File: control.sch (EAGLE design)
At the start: 63 parts

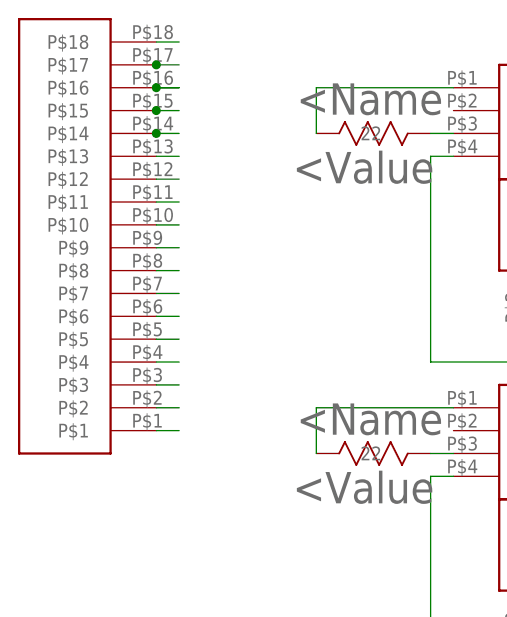
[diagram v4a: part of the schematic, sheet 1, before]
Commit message: Revert "adds flex connector"
This reverts commit c0465f8f5036756819879aef16fe9e16a98b933a.
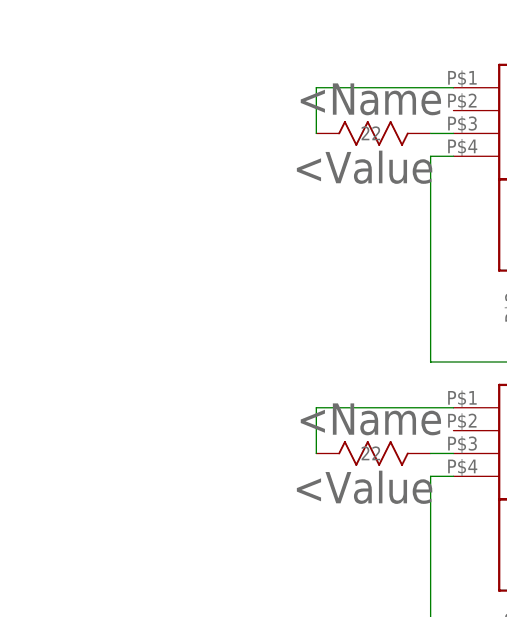
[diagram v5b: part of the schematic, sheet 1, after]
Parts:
- U$39: value SFV18R-3STBE1HLF -> MOTORCONNECTOR; device Smile_Shade:SFV18R-3STBE1HLF -> Smile_Shade:MOTORCONNECTOR
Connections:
- net LEDSTR_1: no longer U$39.P$18
- net LEDSTR_10: no longer U$39.P$9
- net LEDSTR_11: no longer U$39.P$10
- net LEDSTR_12: no longer U$39.P$7
- net LEDSTR_13: no longer U$39.P$6
- net LEDSTR_14: no longer U$39.P$5
- net LEDSTR_15: no longer U$39.P$4
- net LEDSTR_16: no longer U$39.P$3
- net LEDSTR_17: no longer U$39.P$1
- net LEDSTR_18: no longer U$39.P$2
- net LEDSTR_2: no longer U$39.P$17
- net LEDSTR_3: no longer U$39.P$16
- net LEDSTR_4: no longer U$39.P$15
- net LEDSTR_5: no longer U$39.P$12
- net LEDSTR_6: no longer U$39.P$13
- net LEDSTR_7: no longer U$39.P$14
- net LEDSTR_8: no longer U$39.P$11
- net LEDSTR_9: no longer U$39.P$8
- net M1A: now also U$38.MB
- net M1B: now also U$38.MA
- net M2A: now also U$39.MA; no longer U$38.MA
- net M2B: now also U$39.MB; no longer U$38.MB
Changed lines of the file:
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@@
 <part name="U$37" library="Smile_Shade" deviceset="PCA9685PW/Q900" device=""/>
 <part name="U$38" library="Smile_Shade" deviceset="MOTORCONNECTOR" device=""/>
+<part name="U$39" library="Smile_Shade" deviceset="MOTORCONNECTOR" device=""/>
 <part name="U$40" library="LED Driver" deviceset="NUD4011DR2G" device=""/>
 <part name="U$41" library="LED Driver" deviceset="2N7002P" device=""/>
@@
 <part name="U$43" library="LED Driver" deviceset="2N7002P" device=""/>
 <part name="R18" library="LED Driver" deviceset="RC0603FR-0710RL" device=""/>
-<part name="U$39" library="Smile_Shade" deviceset="SFV18R-3STBE1HLF" device=""/>
 </parts>
 <sheets>
@@
 <instance part="U$43" gate="G$1" x="55.88" y="-58.42"/>
 <instance part="R18" gate="A" x="30.48" y="-45.72"/>
-<instance part="U$39" gate="G$1" x="-43.18" y="60.96" rot="R90"/>
 </instances>
 <busses>
@@
 <wire x1="22.86" y1="101.6" x2="25.4" y2="101.6" width="0.1524" layer="91"/>
 </segment>
-<segment>
-<pinref part="U$39" gate="G$1" pin="P$18"/>
-<wire x1="-38.1" y1="106.68" x2="-35.56" y2="106.68" width="0.1524" layer="91"/>
-</segment>
 </net>
 <net name="N$15" class="0">
@@
 <wire x1="73.66" y1="101.6" x2="76.2" y2="101.6" width="0.1524" layer="91"/>
 </segment>
-<segment>
-<wire x1="-38.1" y1="104.14" x2="-35.56" y2="104.14" width="0.1524" layer="91"/>
-<pinref part="U$39" gate="G$1" pin="P$17"/>
-<junction x="-38.1" y="104.14"/>
-</segment>
 </net>
 <net name="N$1" class="0">
@@
 <wire x1="121.92" y1="101.6" x2="124.46" y2="101.6" width="0.1524" layer="91"/>
 </segment>
-<segment>
-<wire x1="-38.1" y1="101.6" x2="-35.56" y2="101.6" width="0.1524" layer="91"/>
-<wire x1="-38.1" y1="101.6" x2="-35.56" y2="101.6" width="0.1524" layer="91"/>
-<pinref part="U$39" gate="G$1" pin="P$16"/>
-<junction x="-38.1" y="101.6"/>
-</segment>
 </net>
 <net name="N$3" class="0">
@@
 <wire x1="172.72" y1="101.6" x2="175.26" y2="101.6" width="0.1524" layer="91"/>
 </segment>
-<segment>
-<wire x1="-38.1" y1="99.06" x2="-35.56" y2="99.06" width="0.1524" layer="91"/>
-<pinref part="U$39" gate="G$1" pin="P$15"/>
-<junction x="-38.1" y="99.06"/>
-</segment>
 </net>
 <net name="N$5" class="0">
@@
 <wire x1="22.86" y1="66.04" x2="25.4" y2="66.04" width="0.1524" layer="91"/>
 </segment>
-<segment>
-<pinref part="U$39" gate="G$1" pin="P$12"/>
-<wire x1="-38.1" y1="91.44" x2="-35.56" y2="91.44" width="0.1524" layer="91"/>
-</segment>
 </net>
 <net name="N$7" class="0">
@@
 <wire x1="73.66" y1="66.04" x2="76.2" y2="66.04" width="0.1524" layer="91"/>
 </segment>
-<segment>
-<pinref part="U$39" gate="G$1" pin="P$13"/>
-<wire x1="-38.1" y1="93.98" x2="-35.56" y2="93.98" width="0.1524" layer="91"/>
-</segment>
 </net>
 <net name="N$9" class="0">
@@
 <wire x1="121.92" y1="66.04" x2="124.46" y2="66.04" width="0.1524" layer="91"/>
 </segment>
-<segment>
-<wire x1="-38.1" y1="96.52" x2="-35.56" y2="96.52" width="0.1524" layer="91"/>
-<pinref part="U$39" gate="G$1" pin="P$14"/>
-<junction x="-38.1" y="96.52"/>
-</segment>
 </net>
 <net name="N$11" class="0">
@@
 <wire x1="172.72" y1="66.04" x2="175.26" y2="66.04" width="0.1524" layer="91"/>
 </segment>
-<segment>
-<pinref part="U$39" gate="G$1" pin="P$11"/>
-<wire x1="-38.1" y1="88.9" x2="-35.56" y2="88.9" width="0.1524" layer="91"/>
-</segment>
 </net>
 <net name="N$13" class="0">
@@
 <wire x1="22.86" y1="30.48" x2="25.4" y2="30.48" width="0.1524" layer="91"/>
 </segment>
-<segment>
-<pinref part="U$39" gate="G$1" pin="P$8"/>
-<wire x1="-38.1" y1="81.28" x2="-35.56" y2="81.28" width="0.1524" layer="91"/>
-</segment>
 </net>
 <net name="N$17" class="0">
@@
 <wire x1="73.66" y1="30.48" x2="76.2" y2="30.48" width="0.1524" layer="91"/>
 </segment>
-<segment>
-<pinref part="U$39" gate="G$1" pin="P$9"/>
-<wire x1="-38.1" y1="83.82" x2="-35.56" y2="83.82" width="0.1524" layer="91"/>
-</segment>
 </net>
 <net name="N$19" class="0">
@@
 <wire x1="121.92" y1="30.48" x2="124.46" y2="30.48" width="0.1524" layer="91"/>
 </segment>
-<segment>
-<pinref part="U$39" gate="G$1" pin="P$10"/>
-<wire x1="-38.1" y1="86.36" x2="-35.56" y2="86.36" width="0.1524" layer="91"/>
-</segment>
 </net>
 <net name="N$21" class="0">
@@
 <wire x1="172.72" y1="30.48" x2="175.26" y2="30.48" width="0.1524" layer="91"/>
 </segment>
-<segment>
-<pinref part="U$39" gate="G$1" pin="P$7"/>
-<wire x1="-38.1" y1="78.74" x2="-35.56" y2="78.74" width="0.1524" layer="91"/>
-</segment>
 </net>
 <net name="N$23" class="0">
@@
 <wire x1="22.86" y1="-5.08" x2="25.4" y2="-5.08" width="0.1524" layer="91"/>
 </segment>
-<segment>
-<pinref part="U$39" gate="G$1" pin="P$6"/>
-<wire x1="-38.1" y1="76.2" x2="-35.56" y2="76.2" width="0.1524" layer="91"/>
-</segment>
 </net>
 <net name="N$25" class="0">
@@
 <wire x1="73.66" y1="-5.08" x2="76.2" y2="-5.08" width="0.1524" layer="91"/>
 </segment>
-<segment>
-<pinref part="U$39" gate="G$1" pin="P$5"/>
-<wire x1="-38.1" y1="73.66" x2="-35.56" y2="73.66" width="0.1524" layer="91"/>
-</segment>
 </net>
 <net name="N$27" class="0">
@@
 <wire x1="121.92" y1="-5.08" x2="124.46" y2="-5.08" width="0.1524" layer="91"/>
 </segment>
-<segment>
-<pinref part="U$39" gate="G$1" pin="P$4"/>
-<wire x1="-38.1" y1="71.12" x2="-35.56" y2="71.12" width="0.1524" layer="91"/>
-</segment>
 </net>
 <net name="N$29" class="0">
@@
 <wire x1="172.72" y1="-5.08" x2="175.26" y2="-5.08" width="0.1524" layer="91"/>
 </segment>
-<segment>
-<pinref part="U$39" gate="G$1" pin="P$3"/>
-<wire x1="-38.1" y1="68.58" x2="-35.56" y2="68.58" width="0.1524" layer="91"/>
-</segment>
 </net>
 <net name="N$31" class="0">
@@
 <wire x1="22.86" y1="-40.64" x2="25.4" y2="-40.64" width="0.1524" layer="91"/>
 </segment>
-<segment>
-<pinref part="U$39" gate="G$1" pin="P$1"/>
-<wire x1="-38.1" y1="63.5" x2="-35.56" y2="63.5" width="0.1524" layer="91"/>
-</segment>
 </net>
 <net name="N$35" class="0">
@@
 <wire x1="73.66" y1="-40.64" x2="76.2" y2="-40.64" width="0.1524" layer="91"/>
 </segment>
-<segment>
-<pinref part="U$39" gate="G$1" pin="P$2"/>
-<wire x1="-38.1" y1="66.04" x2="-35.56" y2="66.04" width="0.1524" layer="91"/>
-</segment>
 </net>
 <net name="N$37" class="0">
@@
 <instance part="C2" gate="A" x="104.14" y="68.58"/>
 <instance part="U$37" gate="G$1" x="213.36" y="43.18"/>
-<instance part="U$38" gate="G$1" x="218.44" y="27.94"/>
+<instance part="U$38" gate="G$1" x="76.2" y="25.4" rot="R180"/>
+<instance part="U$39" gate="G$1" x="218.44" y="27.94"/>
 </instances>
 <busses>
@@
 <segment>
 <wire x1="83.82" y1="30.48" x2="83.82" y2="27.94" width="0.1524" layer="91"/>
+<pinref part="U$38" gate="G$1" pin="MB"/>
+<wire x1="83.82" y1="27.94" x2="81.28" y2="27.94" width="0.1524" layer="91"/>
 <pinref part="U$2" gate="A" pin="1Y"/>
 <wire x1="83.82" y1="30.48" x2="88.9" y2="30.48" width="0.1524" layer="91"/>
@@
 <net name="M2B" class="0">
 <segment>
+<pinref part="U$39" gate="G$1" pin="MB"/>
 <wire x1="213.36" y1="25.4" x2="213.36" y2="22.86" width="0.1524" layer="91"/>
 <pinref part="U$2" gate="A" pin="3Y"/>
 <wire x1="205.74" y1="22.86" x2="213.36" y2="22.86" width="0.1524" layer="91"/>
-<pinref part="U$38" gate="G$1" pin="MB"/>
 </segment>
 </net>
@@
 <wire x1="88.9" y1="22.86" x2="83.82" y2="22.86" width="0.1524" layer="91"/>
 <wire x1="83.82" y1="22.86" x2="83.82" y2="25.4" width="0.1524" layer="91"/>
+<pinref part="U$38" gate="G$1" pin="MA"/>
+<wire x1="83.82" y1="25.4" x2="81.28" y2="25.4" width="0.1524" layer="91"/>
 </segment>
 </net>
@@
 <segment>
 <pinref part="U$2" gate="A" pin="4Y"/>
+<pinref part="U$39" gate="G$1" pin="MA"/>
 <wire x1="205.74" y1="30.48" x2="213.36" y2="30.48" width="0.1524" layer="91"/>
 <wire x1="213.36" y1="30.48" x2="213.36" y2="27.94" width="0.1524" layer="91"/>
-<pinref part="U$38" gate="G$1" pin="MA"/>
-</segment>
-</net>
+</segment>
+</net>
